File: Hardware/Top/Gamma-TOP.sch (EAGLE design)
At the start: 58 parts, among them SW1 SWITCH.MOM, SW2 SWITCH.MOM, U1 FT231XS, U3 NRF52832_MODULE_MDBT42, Y1 32.768kHz

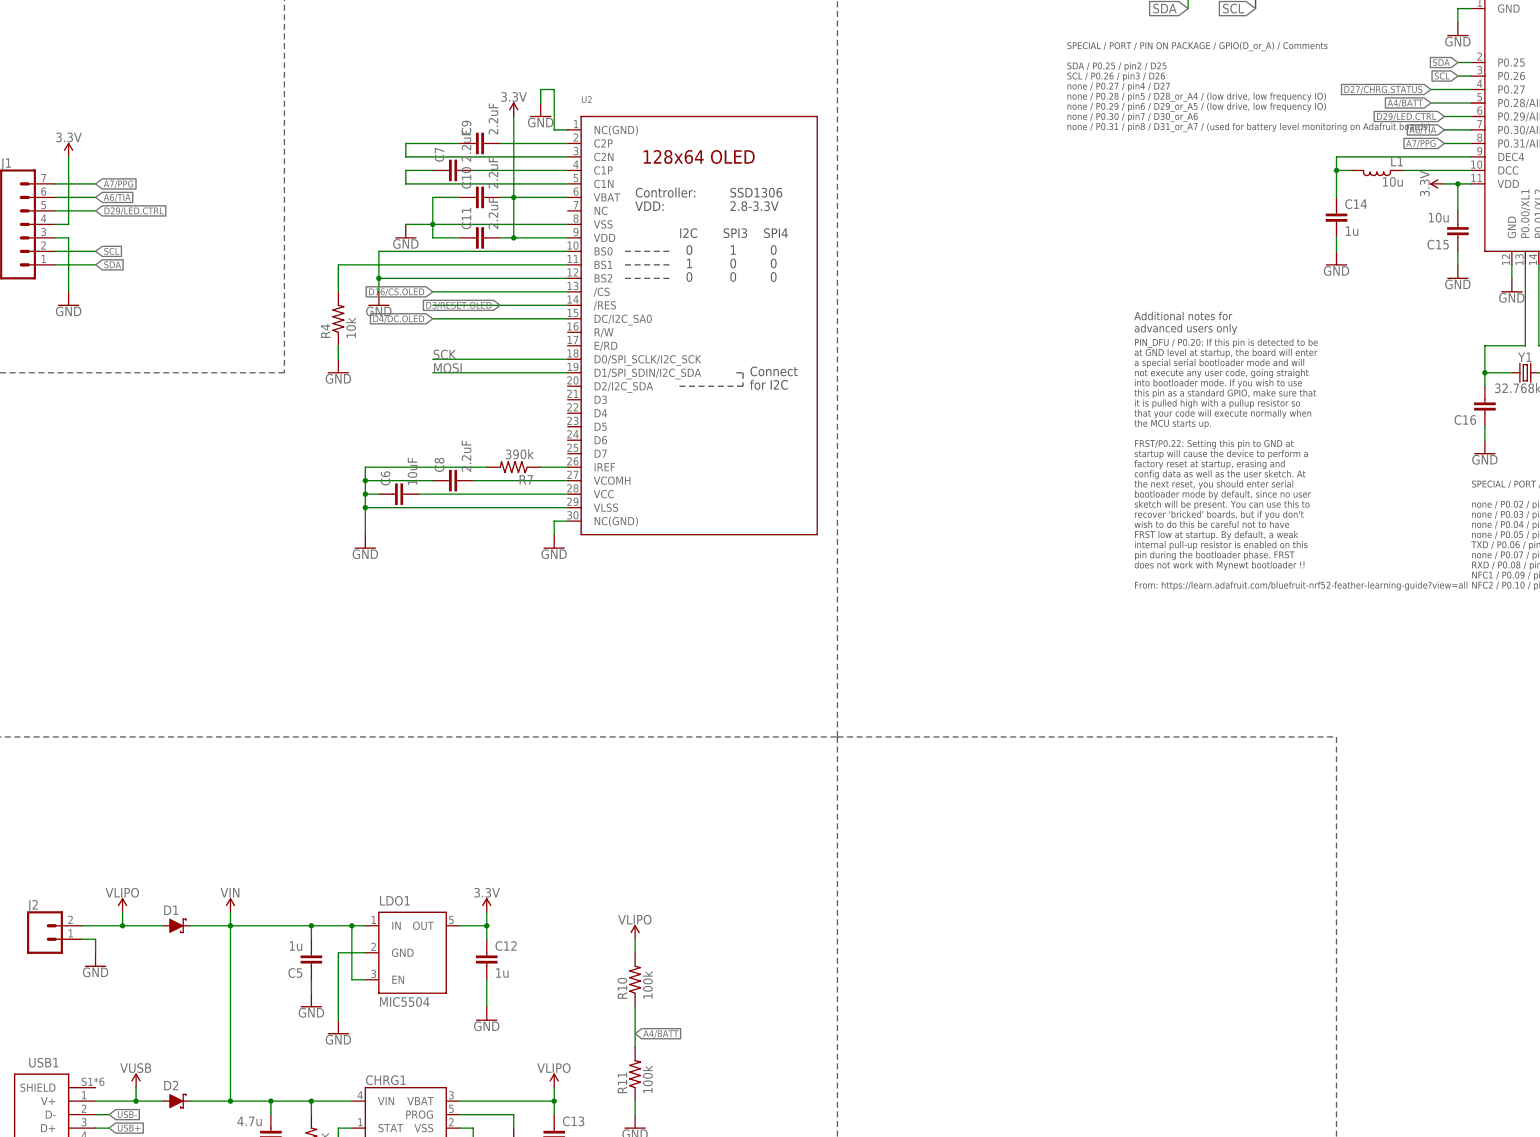
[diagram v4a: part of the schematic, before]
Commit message: Take 007 35:16, before I attempt to move the power circuit on bottom of Top board out to the outside regions
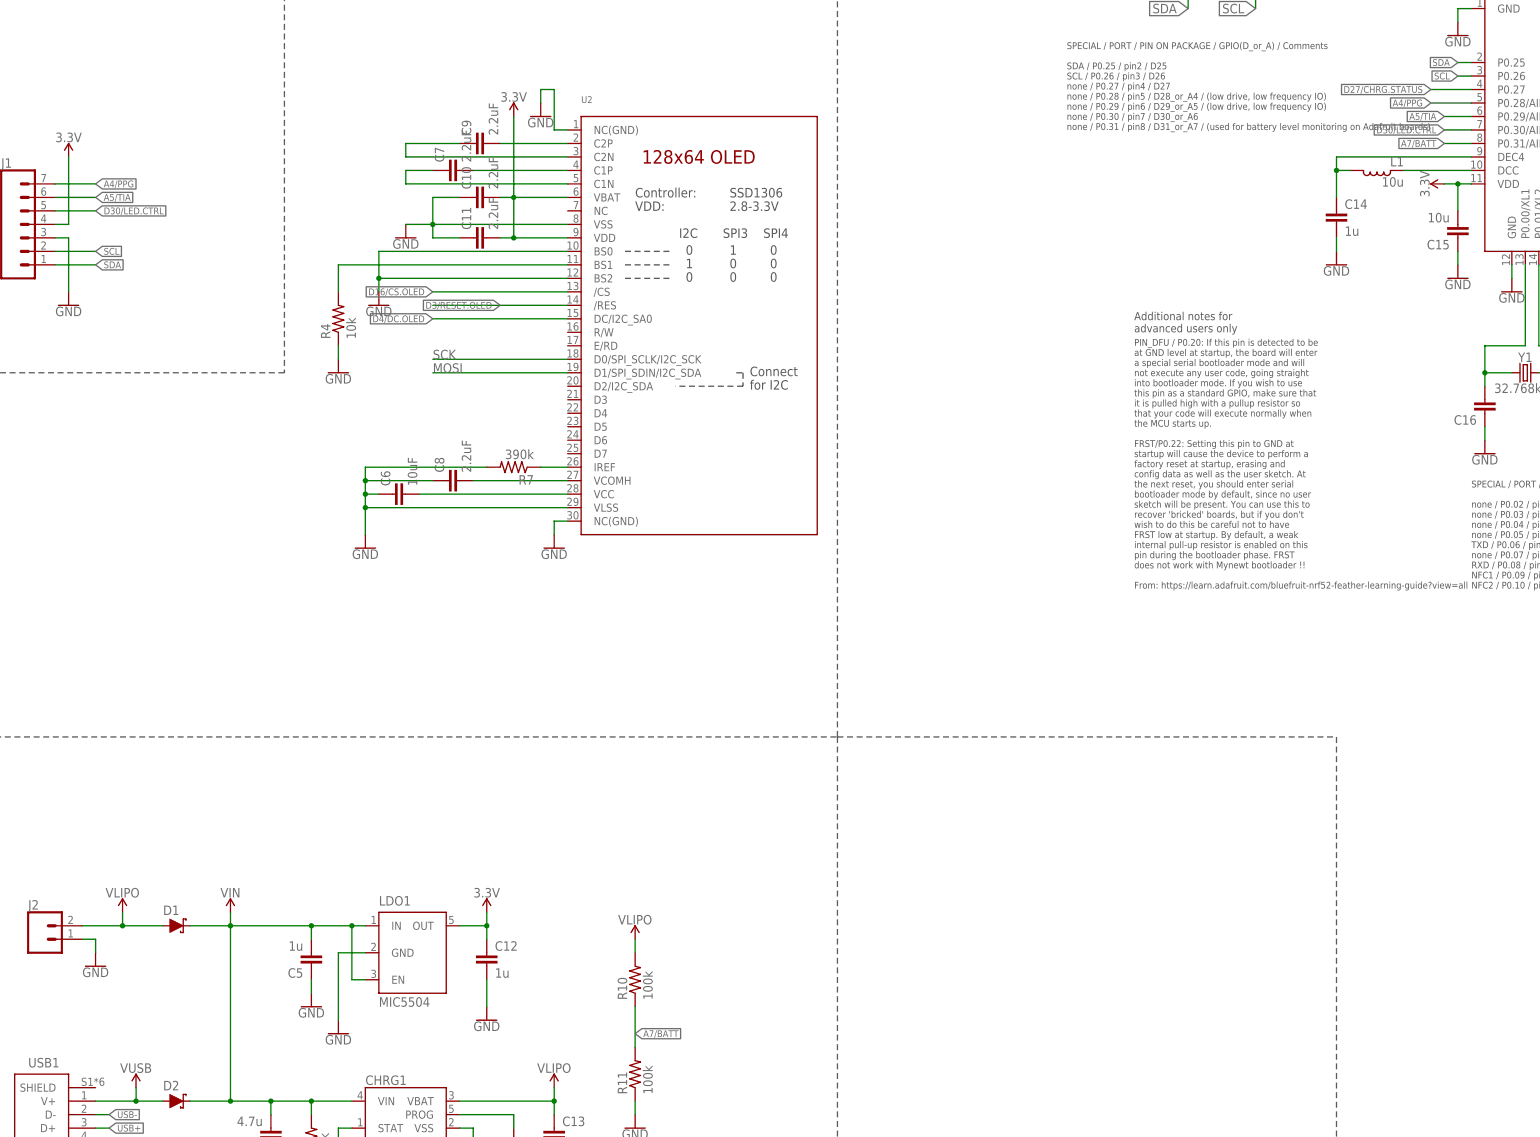
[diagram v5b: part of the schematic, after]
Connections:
- removed net A4/BATT: R10.1, R11.2, U3.P0.28/AIN4
- removed net A6/TIA: J1.6, U3.P0.30/AIN6
- removed net A7/PPG: J1.7, U3.P0.31/AIN7
- removed net D29/LED.CTRL: J1.5, U3.P0.29/AIN5
- new net A4/PPG: J1.7, U3.P0.28/AIN4
- new net A5/TIA: J1.6, U3.P0.29/AIN5
- new net A7/BATT: R10.1, R11.2, U3.P0.31/AIN7
- new net D30/LED.CTRL: J1.5, U3.P0.30/AIN6
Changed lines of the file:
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@@
 </segment>
 </net>
-<net name="A4/BATT" class="0">
+<net name="A4/PPG" class="0">
 <segment>
 <pinref part="U3" gate="G$1" pin="P0.28/AIN4"/>
@@
 </segment>
 <segment>
-<pinref part="R10" gate="G$1" pin="1"/>
-<pinref part="R11" gate="G$1" pin="2"/>
-<wire x1="-88.9" y1="-81.28" x2="-88.9" y2="-73.66" width="0.1524" layer="91"/>
-<label x="-88.9" y="-78.74" size="1.27" layer="95" xref="yes"/>
+<pinref part="J1" gate="G$1" pin="7"/>
+<wire x1="-198.12" y1="81.28" x2="-190.5" y2="81.28" width="0.1524" layer="91"/>
+<label x="-190.5" y="81.28" size="1.27" layer="95" xref="yes"/>
 </segment>
 </net>
@@
 </segment>
 </net>
-<net name="D29/LED.CTRL" class="0">
+<net name="A5/TIA" class="0">
 <segment>
 <pinref part="U3" gate="G$1" pin="P0.29/AIN5"/>
 <wire x1="68.58" y1="93.98" x2="63.5" y2="93.98" width="0.1524" layer="91"/>
 <label x="63.5" y="93.98" size="1.27" layer="95" rot="R180" xref="yes"/>
+</segment>
+<segment>
+<pinref part="J1" gate="G$1" pin="6"/>
+<wire x1="-198.12" y1="78.74" x2="-190.5" y2="78.74" width="0.1524" layer="91"/>
+<label x="-190.5" y="78.74" size="1.27" layer="95" xref="yes"/>
+</segment>
+</net>
+<net name="A7/BATT" class="0">
+<segment>
+<pinref part="U3" gate="G$1" pin="P0.31/AIN7"/>
+<wire x1="68.58" y1="88.9" x2="63.5" y2="88.9" width="0.1524" layer="91"/>
+<label x="63.5" y="88.9" size="1.27" layer="95" rot="R180" xref="yes"/>
+</segment>
+<segment>
+<pinref part="R10" gate="G$1" pin="1"/>
+<pinref part="R11" gate="G$1" pin="2"/>
+<wire x1="-88.9" y1="-81.28" x2="-88.9" y2="-73.66" width="0.1524" layer="91"/>
+<label x="-88.9" y="-78.74" size="1.27" layer="95" xref="yes"/>
+</segment>
+</net>
+<net name="D30/LED.CTRL" class="0">
+<segment>
+<pinref part="U3" gate="G$1" pin="P0.30/AIN6"/>
+<wire x1="68.58" y1="91.44" x2="63.5" y2="91.44" width="0.1524" layer="91"/>
+<label x="63.5" y="91.44" size="1.27" layer="95" rot="R180" xref="yes"/>
 </segment>
 <segment>
@@
 </segment>
 </net>
-<net name="A6/TIA" class="0">
-<segment>
-<pinref part="U3" gate="G$1" pin="P0.30/AIN6"/>
-<wire x1="68.58" y1="91.44" x2="63.5" y2="91.44" width="0.1524" layer="91"/>
-<label x="63.5" y="91.44" size="1.27" layer="95" rot="R180" xref="yes"/>
-</segment>
-<segment>
-<pinref part="J1" gate="G$1" pin="6"/>
-<wire x1="-198.12" y1="78.74" x2="-190.5" y2="78.74" width="0.1524" layer="91"/>
-<label x="-190.5" y="78.74" size="1.27" layer="95" xref="yes"/>
-</segment>
-</net>
-<net name="A7/PPG" class="0">
-<segment>
-<pinref part="U3" gate="G$1" pin="P0.31/AIN7"/>
-<wire x1="68.58" y1="88.9" x2="63.5" y2="88.9" width="0.1524" layer="91"/>
-<label x="63.5" y="88.9" size="1.27" layer="95" rot="R180" xref="yes"/>
-</segment>
-<segment>
-<pinref part="J1" gate="G$1" pin="7"/>
-<wire x1="-198.12" y1="81.28" x2="-190.5" y2="81.28" width="0.1524" layer="91"/>
-<label x="-190.5" y="81.28" size="1.27" layer="95" xref="yes"/>
-</segment>
-</net>

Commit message: Finished with Preliminary Version A of Smartwatch as of end of Take 008 video
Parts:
- R8: value (none) -> 5k
- renumbered SW3 to RESET
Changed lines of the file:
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@@
 <part name="SW4" library="LinnesLab-Switches" deviceset="SPST-PTS830GG140-COPY" device=".1-3" package3d_urn="urn:adsk.eagle:package:18580190/2"/>
 <part name="GND30" library="LinnesLab-Symbols" deviceset="GND" device=""/>
-<part name="SW3" library="LinnesLab-Switches" deviceset="SPST-PTS830GG140-COPY" device=".1-3" package3d_urn="urn:adsk.eagle:package:18580190/2"/>
+<part name="RESET" library="LinnesLab-Switches" deviceset="SPST-PTS830GG140-COPY" device=".1-3" package3d_urn="urn:adsk.eagle:package:18580190/2"/>
 <part name="U3" library="LinnesLab-Microcontrollers" deviceset="NRF52832_MODULE_MDBT42" device="" override_package3d_urn="urn:adsk.eagle:package:18593121/2" override_package_urn="urn:adsk.eagle:footprint:18593122/1"/>
 <part name="LED1" library="LinnesLab-LED" deviceset="LED" device="0603" package3d_urn="urn:adsk.eagle:package:18593052/2" value="RED"/>
@@
 <part name="C13" library="LinnesLab-Passives" deviceset="CAPACITOR" device="0603" package3d_urn="urn:adsk.eagle:package:15661989/2" value="4.7u"/>
 <part name="C4" library="LinnesLab-Passives" deviceset="CAPACITOR" device="0603" package3d_urn="urn:adsk.eagle:package:15661989/2" value="4.7u"/>
-<part name="R8" library="LinnesLab-Passives" deviceset="RESISTOR" device="0603" package3d_urn="urn:adsk.eagle:package:15661944/2"/>
+<part name="R8" library="LinnesLab-Passives" deviceset="RESISTOR" device="0603" package3d_urn="urn:adsk.eagle:package:15661944/2" value="5k"/>
 <part name="R3" library="LinnesLab-Passives" deviceset="RESISTOR" device="0603" package3d_urn="urn:adsk.eagle:package:15661944/2" value="100k"/>
 <part name="GND34" library="LinnesLab-Symbols" deviceset="GND" device=""/>
@@
 <attribute name="VALUE" x="76.2" y="60.706" size="1.778" layer="96" align="top-center"/>
 </instance>
-<instance part="SW3" gate="G$1" x="320.04" y="20.32" smashed="yes">
+<instance part="RESET" gate="G$1" x="320.04" y="20.32" smashed="yes">
 <attribute name="NAME" x="317.5" y="17.78" size="1.27" layer="95"/>
 <attribute name="VALUE" x="317.5" y="15.24" size="1.27" layer="96"/>
@@
 <wire x1="327.66" y1="20.32" x2="327.66" y2="17.78" width="0.1524" layer="91"/>
 <pinref part="GND28" gate="G$1" pin="GND"/>
-<pinref part="SW3" gate="G$1" pin="B"/>
+<pinref part="RESET" gate="G$1" pin="B"/>
 </segment>
 <segment>
@@
 <wire x1="312.42" y1="20.32" x2="314.96" y2="20.32" width="0.1524" layer="91"/>
 <label x="312.42" y="20.32" size="1.27" layer="95" rot="R180" xref="yes"/>
-<pinref part="SW3" gate="G$1" pin="A"/>
-</segment>
-<segment>
+<pinref part="RESET" gate="G$1" pin="A"/>
+</segment>
+<segment>

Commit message: Updated file names and completed preliminary BOM for each board
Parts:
- added C18, C21: 120p, LinnesLab-Passives:CAPACITOR0603
- added C19: 100n, LinnesLab-Passives:CAPACITOR0603
- added NFCANTENNA: 2.1 uH, NFC-Antenna:MOLEX-1462360151-ANTENNA
- added U5: FT24C64A, LinnesLab-DigitalIC:FT24C64A
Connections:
- new net WP: U3.P0.02/AIN0, U5.WP
- net 3.3V: now also C19.1, U5.VCC
- net GND: now also C18.2, C19.2, C21.2, U5.GND
- net P0.09/NFC1: now also C18.1, NFCANTENNA.NFC1
- net P0.10/NFC2: now also C21.1, NFCANTENNA.NFC2
- net SCL: now also U5.SCL
- net SDA: now also U5.SDA
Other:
- note added: "EEPROM Storage"
- note added: "Gamma Top Version B (Full Version)"
- note added: "NFC Tuning Circuit with Antenna"
- note removed: "Gamma Top Version A"
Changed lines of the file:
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@@
 <part name="SUPPLY8" library="LinnesLab-Symbols" deviceset="3.3V" device=""/>
 <part name="GND6" library="LinnesLab-Symbols" deviceset="GND" device=""/>
+<part name="U5" library="LinnesLab-DigitalIC" deviceset="FT24C64A" device="" package3d_urn="urn:adsk.eagle:package:18172171/2"/>
+<part name="SUPPLY10" library="LinnesLab-Symbols" deviceset="3.3V" device=""/>
+<part name="GND5" library="LinnesLab-Symbols" deviceset="GND" device=""/>
+<part name="C19" library="LinnesLab-Passives" deviceset="CAPACITOR" device="0603" package3d_urn="urn:adsk.eagle:package:15661989/2" value="100n"/>
+<part name="SUPPLY11" library="LinnesLab-Symbols" deviceset="3.3V" device=""/>
+<part name="GND13" library="LinnesLab-Symbols" deviceset="GND" device=""/>
+<part name="NFCANTENNA" library="NFC-Antenna" deviceset="MOLEX-1462360151-ANTENNA" device="" value="2.1 uH"/>
+<part name="GND2" library="LinnesLab-Symbols" deviceset="GND" device=""/>
+<part name="GND4" library="LinnesLab-Symbols" deviceset="GND" device=""/>
+<part name="C18" library="LinnesLab-Passives" deviceset="CAPACITOR" device="0603" package3d_urn="urn:adsk.eagle:package:15661989/2" value="120p"/>
+<part name="C21" library="LinnesLab-Passives" deviceset="CAPACITOR" device="0603" package3d_urn="urn:adsk.eagle:package:15661989/2" value="120p"/>
 </parts>
 <sheets>
@@
 <wire x1="360.68" y1="68.58" x2="261.62" y2="68.58" width="0.1524" layer="97" style="dashdot"/>
 <wire x1="261.62" y1="142.24" x2="360.68" y2="142.24" width="0.1524" layer="97" style="dashdot"/>
-<text x="35.56" y="205.74" size="10.16" layer="90">Gamma Top Version A</text>
+<text x="35.56" y="205.74" size="10.16" layer="90">Gamma Top Version B (Full Version)</text>
+<text x="-30.48" y="-43.18" size="5.08" layer="90">EEPROM Storage</text>
+<text x="269.24" y="-50.8" size="4.572" layer="90">NFC Tuning Circuit with Antenna</text>
 </plain>
 <instances>
@@
 <instance part="GND6" gate="G$1" x="-195.58" y="58.42" smashed="yes">
 <attribute name="VALUE" x="-195.58" y="58.166" size="1.778" layer="96" align="top-center"/>
+</instance>
+<instance part="U5" gate="G$1" x="-10.16" y="-78.74" smashed="yes">
+<attribute name="NAME" x="-17.78" y="-72.39" size="1.778" layer="95"/>
+<attribute name="VALUE" x="-17.78" y="-86.36" size="1.778" layer="96"/>
+</instance>
+<instance part="SUPPLY10" gate="G$1" x="2.54" y="-73.66" smashed="yes">
+<attribute name="VALUE" x="2.54" y="-70.866" size="1.778" layer="96" align="bottom-center"/>
+</instance>
+<instance part="GND5" gate="G$1" x="2.54" y="-86.36" smashed="yes">
+<attribute name="VALUE" x="2.54" y="-86.614" size="1.778" layer="96" align="top-center"/>
+</instance>
+<instance part="C19" gate="G$1" x="10.16" y="-78.74" smashed="yes">
+<attribute name="NAME" x="11.684" y="-75.819" size="1.778" layer="95"/>
+<attribute name="VALUE" x="11.684" y="-80.899" size="1.778" layer="96"/>
+</instance>
+<instance part="SUPPLY11" gate="G$1" x="10.16" y="-71.12" smashed="yes">
+<attribute name="VALUE" x="10.16" y="-68.326" size="1.778" layer="96" align="bottom-center"/>
+</instance>
+<instance part="GND13" gate="G$1" x="10.16" y="-86.36" smashed="yes">
+<attribute name="VALUE" x="10.16" y="-86.614" size="1.778" layer="96" align="top-center"/>
+</instance>
+<instance part="NFCANTENNA" gate="G$1" x="304.8" y="-101.6" smashed="yes" rot="R90">
+<attribute name="NAME" x="294.64" y="-111.76" size="1.778" layer="95" rot="R90"/>
+<attribute name="VALUE" x="317.5" y="-111.76" size="1.778" layer="96" rot="R90"/>
+</instance>
+<instance part="GND2" gate="G$1" x="340.36" y="-86.36" smashed="yes">
+<attribute name="VALUE" x="340.36" y="-86.614" size="1.778" layer="96" align="top-center"/>
+</instance>
+<instance part="GND4" gate="G$1" x="299.72" y="-83.82" smashed="yes">
+<attribute name="VALUE" x="299.72" y="-84.074" size="1.778" layer="96" align="top-center"/>
+</instance>
+<instance part="C18" gate="G$1" x="294.64" y="-78.74" smashed="yes" rot="R90">
+<attribute name="NAME" x="291.719" y="-77.216" size="1.778" layer="95" rot="R90"/>
+<attribute name="VALUE" x="296.799" y="-77.216" size="1.778" layer="96" rot="R90"/>
+</instance>
+<instance part="C21" gate="G$1" x="337.82" y="-78.74" smashed="yes" rot="R90">
+<attribute name="NAME" x="334.899" y="-77.216" size="1.778" layer="95" rot="R90"/>
+<attribute name="VALUE" x="339.979" y="-77.216" size="1.778" layer="96" rot="R90"/>
 </instance>
 </instances>
@@
 <pinref part="GND6" gate="G$1" pin="GND"/>
 </segment>
+<segment>
+<pinref part="U5" gate="G$1" pin="GND"/>
+<wire x1="0" y1="-81.28" x2="2.54" y2="-81.28" width="0.1524" layer="91"/>
+<wire x1="2.54" y1="-81.28" x2="2.54" y2="-83.82" width="0.1524" layer="91"/>
+<pinref part="GND5" gate="G$1" pin="GND"/>
+</segment>
+<segment>
+<pinref part="C19" gate="G$1" pin="2"/>
+<pinref part="GND13" gate="G$1" pin="GND"/>
+<wire x1="10.16" y1="-83.82" x2="10.16" y2="-81.28" width="0.1524" layer="91"/>
+</segment>
+<segment>
+<pinref part="C18" gate="G$1" pin="2"/>
+<pinref part="GND4" gate="G$1" pin="GND"/>
+<wire x1="297.18" y1="-78.74" x2="299.72" y2="-78.74" width="0.1524" layer="91"/>
+<wire x1="299.72" y1="-78.74" x2="299.72" y2="-81.28" width="0.1524" layer="91"/>
+</segment>
+<segment>
+<pinref part="C21" gate="G$1" pin="2"/>
+<pinref part="GND2" gate="G$1" pin="GND"/>
+<wire x1="340.36" y1="-78.74" x2="340.36" y2="-83.82" width="0.1524" layer="91"/>
+</segment>
 </net>
 <net name="SWDIO" class="0">
@@
 <pinref part="SUPPLY8" gate="G$1" pin="3.3V"/>
 </segment>
+<segment>
+<pinref part="U5" gate="G$1" pin="VCC"/>
+<wire x1="0" y1="-76.2" x2="2.54" y2="-76.2" width="0.1524" layer="91"/>
+<wire x1="2.54" y1="-76.2" x2="2.54" y2="-73.66" width="0.1524" layer="91"/>
+<pinref part="SUPPLY10" gate="G$1" pin="3.3V"/>
+</segment>
+<segment>
+<pinref part="C19" gate="G$1" pin="1"/>
+<pinref part="SUPPLY11" gate="G$1" pin="3.3V"/>
+<wire x1="10.16" y1="-73.66" x2="10.16" y2="-71.12" width="0.1524" layer="91"/>
+</segment>
 </net>
 <net name="SDA" class="0">
@@
 <label x="-190.5" y="66.04" size="1.27" layer="95" xref="yes"/>
 </segment>
+<segment>
+<pinref part="U5" gate="G$1" pin="SDA"/>
+<wire x1="-22.86" y1="-76.2" x2="-20.32" y2="-76.2" width="0.1524" layer="91"/>
+<label x="-22.86" y="-76.2" size="1.27" layer="95" rot="R180" xref="yes"/>
+</segment>
 </net>
 <net name="SCL" class="0">
@@
 <wire x1="-198.12" y1="68.58" x2="-190.5" y2="68.58" width="0.1524" layer="91"/>
 <label x="-190.5" y="68.58" size="1.27" layer="95" xref="yes"/>
+</segment>
+<segment>
+<pinref part="U5" gate="G$1" pin="SCL"/>
+<wire x1="-22.86" y1="-78.74" x2="-20.32" y2="-78.74" width="0.1524" layer="91"/>
+<label x="-22.86" y="-78.74" size="1.27" layer="95" rot="R180" xref="yes"/>
 </segment>
 </net>
@@
 <label x="101.6" y="48.26" size="1.27" layer="95" rot="R180" xref="yes"/>
 </segment>
+<segment>
+<wire x1="287.02" y1="-60.96" x2="287.02" y2="-78.74" width="0.1524" layer="91"/>
+<label x="287.02" y="-60.96" size="4.572" layer="95" rot="R180" xref="yes"/>
+<pinref part="C18" gate="G$1" pin="1"/>
+<wire x1="287.02" y1="-78.74" x2="289.56" y2="-78.74" width="0.1524" layer="91"/>
+<wire x1="289.56" y1="-78.74" x2="289.56" y2="-91.44" width="0.1524" layer="91"/>
+<wire x1="289.56" y1="-91.44" x2="302.26" y2="-91.44" width="0.1524" layer="91"/>
+<pinref part="NFCANTENNA" gate="G$1" pin="NFC1"/>
+<wire x1="302.26" y1="-91.44" x2="302.26" y2="-96.52" width="0.1524" layer="91"/>
+</segment>
 </net>
 <net name="SCK" class="0">
@@
 <pinref part="U3" gate="G$1" pin="P0.10"/>
 <label x="104.14" y="48.26" size="1.27" layer="95" xref="yes"/>
+</segment>
+<segment>
+<wire x1="332.74" y1="-60.96" x2="332.74" y2="-78.74" width="0.1524" layer="91"/>
+<label x="332.74" y="-60.96" size="4.572" layer="95" rot="R180" xref="yes"/>
+<pinref part="NFCANTENNA" gate="G$1" pin="NFC2"/>
+<pinref part="C21" gate="G$1" pin="1"/>
+<wire x1="307.34" y1="-96.52" x2="332.74" y2="-96.52" width="0.1524" layer="91"/>
+<wire x1="332.74" y1="-96.52" x2="332.74" y2="-78.74" width="0.1524" layer="91"/>
 </segment>
 </net>
@@
 </segment>
 </net>
+<net name="WP" class="0">
+<segment>
+<pinref part="U5" gate="G$1" pin="WP"/>
+<wire x1="-22.86" y1="-81.28" x2="-20.32" y2="-81.28" width="0.1524" layer="91"/>
+<label x="-22.86" y="-81.28" size="1.27" layer="95" rot="R180" xref="yes"/>
+</segment>
+<segment>
+<pinref part="U3" gate="G$1" pin="P0.02/AIN0"/>
+<wire x1="83.82" y1="66.04" x2="83.82" y2="63.5" width="0.1524" layer="91"/>
+<label x="83.82" y="63.5" size="1.27" layer="95" rot="R270" xref="yes"/>
+</segment>
+</net>
